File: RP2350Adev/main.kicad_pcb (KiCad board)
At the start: 4 copper layers, 88.9 x 50.9 mm, 125 parts, among them J201 J-Link, J202 SPI Pins, J203 QSPI Pins, J204 UART Pins, J401 UART, J402 DEBUG, J701 USB_A_Male, J702 USB_A_Female, J703 USB4105-GF-A, M701 TS3USB3031RMGR, SW701 SW_DIP_x06, U201 nRF5340-QKxx, U302 LFD_Diplexer, U303 nRF7002-QFAA, U401 MCP1702T-3302E_CB, U402 W25Q32JV, U403 RP2350A, U701 TS3USB30EDGSR, X201 32MHz, X202 32.768kHz, X301 XTAL-40, X401 IQXO-791

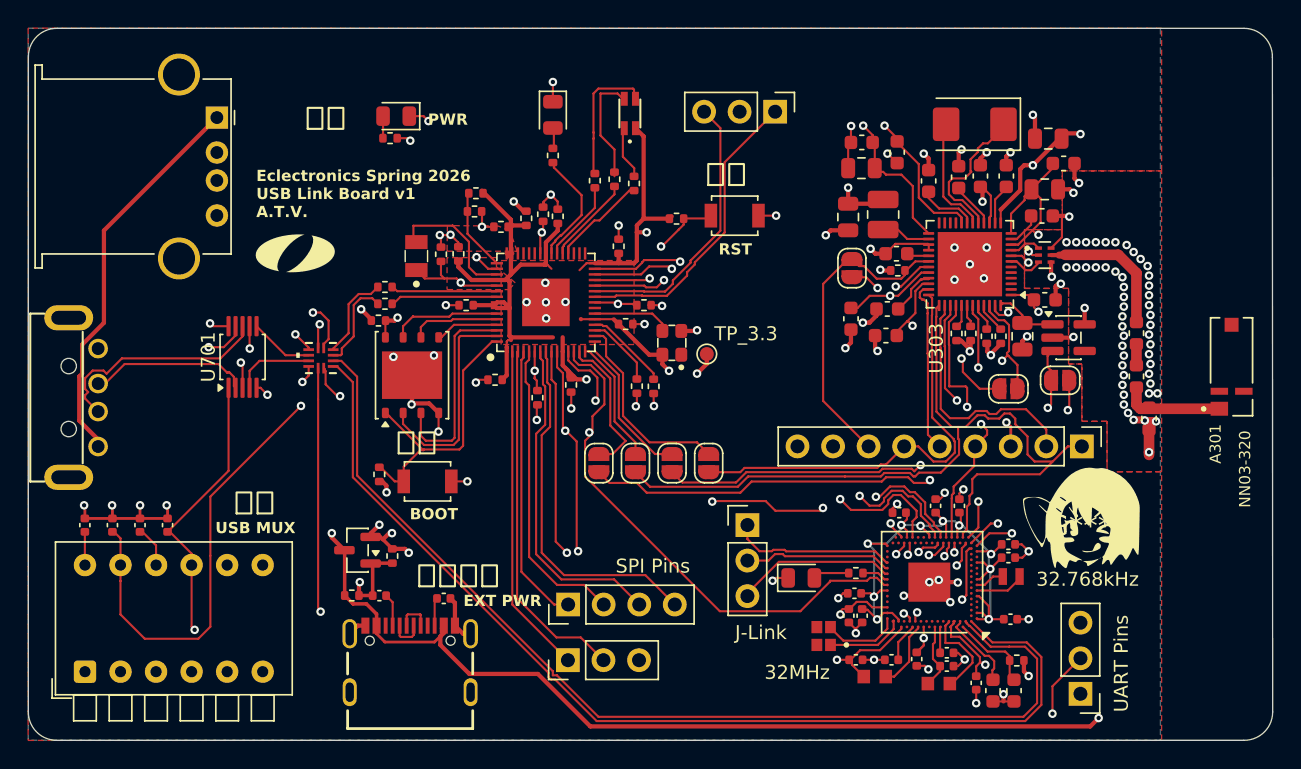
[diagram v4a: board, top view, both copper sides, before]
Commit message: fix footprint errors
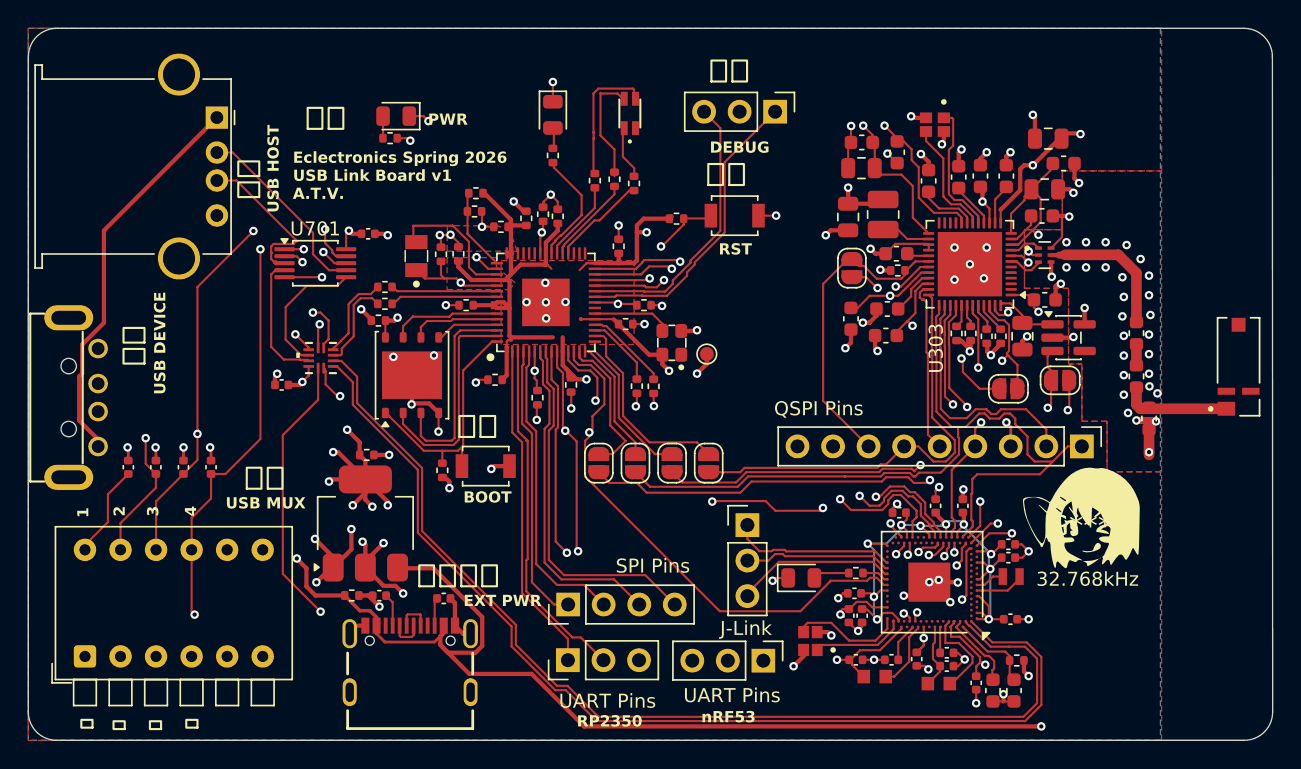
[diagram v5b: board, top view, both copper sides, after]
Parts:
- removed OlinLogo: G***, Eclectronics:OlinLogo
- added C701: 1uF, Capacitor_SMD:C_0402_1005Metric, F.Cu at (68.1, 103.0)
- added C702: 1uF, Capacitor_SMD:C_0402_1005Metric, F.Cu at (61.9, 113.8)
- U301: value ~ -> TCK106AF
- U401: value MCP1702T-3302E_CB -> LD1117S33TR_SOT223; footprint Package_TO_SOT_SMD:SOT-23 -> Package_TO_SOT_SMD:SOT-223-3_TabPin2
- X301: footprint Crystal:Crystal_SMD_Abracon_ABM3-2Pin_5.0x3.2mm -> Eclectronics:XTAL_ABM11W-32.0000MHZ-8-D1X-T3
- moved J204 22.8 mm to (96.3, 133.5), turned to -90 degrees
- moved U701 8.48 mm to (64.3, 105.1), turned to 0 degrees
- moved C403 7.45 mm to (68.0, 118.8), turned to 0 degrees
- moved R701 5.17 mm to (51.0, 119.7)
- moved R702 5.17 mm to (52.9, 119.7)
- moved R703 5.17 mm to (54.9, 119.7)
- moved R704 5.17 mm to (56.9, 119.7)
- moved R402 4.51 mm to (73.4, 119.9)
- moved S402 4.30 mm to (76.5, 119.6)
- moved G*** 3.18 mm to (70.2, 116.0)
- moved X301 2.85 mm to (108.6, 95.2), turned to -90 degrees
- moved U401 1.99 mm to (67.9, 123.7), turned to 90 degrees
- moved SW701 1.09 mm to (47.9, 133.2)
- moved X201 1.02 mm to (99.7, 132.1)
- moved A301 0.50 mm to (130.3, 112.5)
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- renumbered TP_3.3 to TP101
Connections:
- X201 pad 2: Net-(U201-XC1) -> GND
- X201 pad 3: (no net) -> Net-(U201-XC1)
- X201 pad 4: (no net) -> GND
- X301 pad 2: Net-(U303-XON) -> GND
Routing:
- net /RP2350Adev/MUX2_OE: track 101.1 -> 128.1 mm, vias 4 -> 6
- net +3V3: track 171.9 -> 186.8 mm, vias 31 -> 37
- net /RP2350Adev/MUX2_S: track 117.6 -> 131.5 mm, vias 3 -> 5
- net /RP2350Adev/MUX1_S1: track 89.4 -> 78.7 mm
- net Net-(J701-D+): track 11.5 -> 21.1 mm, vias 0 -> 1
- net GND: track 132.4 -> 139.6 mm, vias 131 -> 119
- net Net-(J701-D-): track 16.4 -> 23.5 mm, vias 0 -> 1
- net /RP2350Adev/MUX1_S0: track 101.5 -> 107.9 mm
- net /nRF5340/RX: track 22.1 -> 16.2 mm, vias 2 -> 1
- net Net-(M701-D-): track 4.58 -> 9.65 mm
- net Net-(J702-D+): track 15.6 -> 11.8 mm, vias 1 -> 0
- net Net-(M701-D+): track 5.73 -> 9.37 mm
- net Net-(J702-D-): track 16.6 -> 13.6 mm, vias 1 -> 0
- net /RP2350Adev/BOOT: track 21.0 -> 18.3 mm
- net /nRF5340/QSPI1: track 61.5 -> 58.8 mm
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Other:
- board text added: "1"
- board text added: "2"
- board text added: "3"
- board text added: "4"
- board text added: "Allan Huang Trinity Lee Venkadesh Eswaranandam"
- board text added: "DEBUG"
- board text added: "QSPI Pins"
- board text added: "RP2350"
- board text added: "UART Pins"
- board text added: "USB DEVICE"
- board text added: "USB HOST"
- board text added: "nRF53"
- board text added: "一"
- board text added: "三"
- board text added: "主機"
- board text added: "二"
- board text added: "四"
- board text added: "裝置"
- board text added: "除錯"
- board text removed: "Allan Huang Trinity Lee Venkadesh Eswaranadam"

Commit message: Add silk
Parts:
- moved D403 18.5 mm to (95.8, 110.6), turned to 180 degrees
- moved TP101 3.99 mm to (90.4, 115.1)
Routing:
- net Net-(D403-Pad1): track 3.78 -> 19.7 mm, vias 0 -> 2
- net Net-(D403-Pad4): track 9.66 -> 23.8 mm, vias 0 -> 2
- net Net-(D403-Pad2): track 8.09 -> 21.7 mm, vias 0 -> 2
- net +3V3: track 186.8 -> 186.6 mm, vias 37 -> 38
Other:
- board text added: "ANTenna"
- board text added: "FAULT"
- board text added: "STATUS"
- board text added: "狀態"
- board text added: "錯誤"
- board text added: "開關"

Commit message: final fab files
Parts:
- moved R701 1.44 mm to (52.4, 119.6)
- moved R702 0.77 mm to (53.7, 119.7)
- moved J703 0.55 mm to (71.1, 136.3)
- moved L401 0.14 mm to (71.4, 104.6)
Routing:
- net GND: track 139.6 -> 155.6 mm
- net +3V3: track 186.6 -> 190.3 mm
- net /RP2350Adev/MUX2_S: track 131.5 -> 134.7 mm
- net +5V: track 127.4 -> 125.3 mm
- net unconnected-(J703-D--PadA7): track 2.49 -> 4.00 mm
- net /RP2350Adev/MUX1_S0: track 107.9 -> 109.0 mm
- net unconnected-(J703-D+-PadA6): track 2.55 -> 3.50 mm
- net Net-(U301-VOUT): track 4.70 -> 5.23 mm
